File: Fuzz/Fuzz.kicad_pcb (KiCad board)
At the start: 2 copper layers, 13 parts, among them Q1 BC108, Q2 BC108, U3 TL071

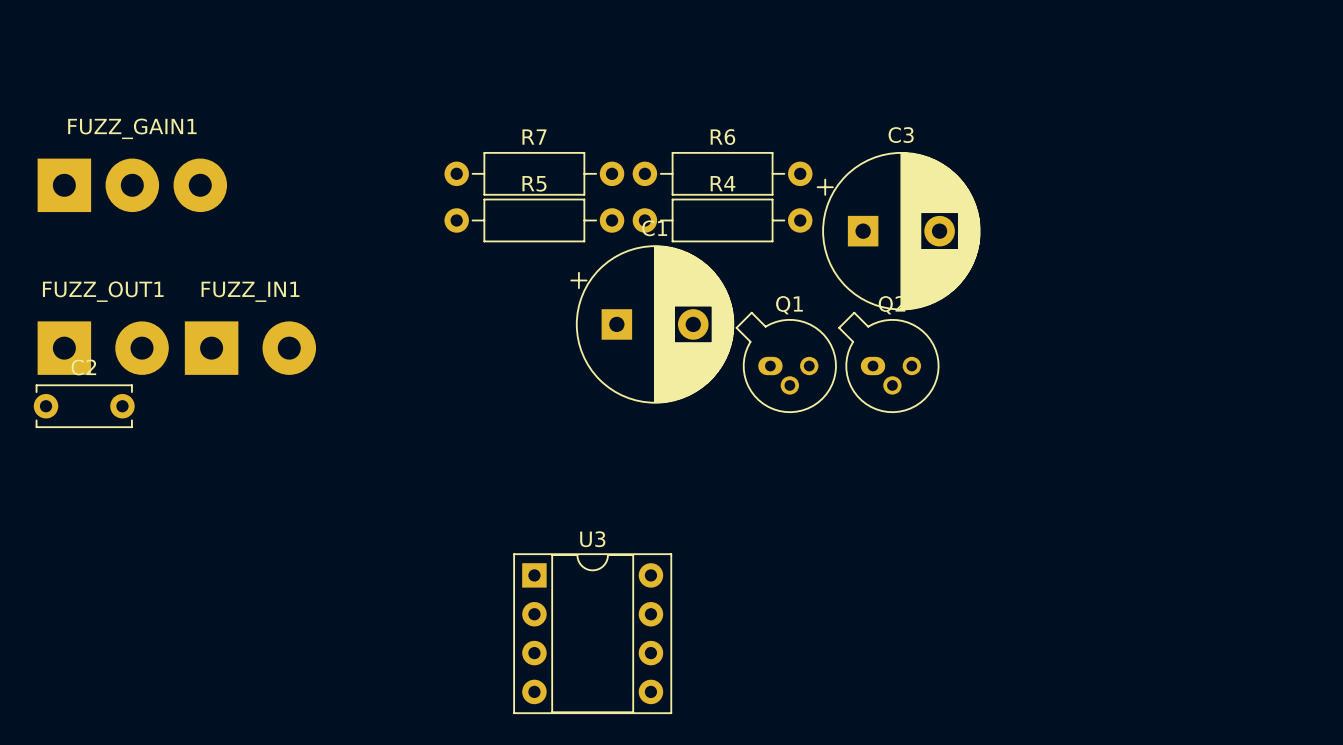
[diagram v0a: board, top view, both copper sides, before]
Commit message: Arrange pcb components
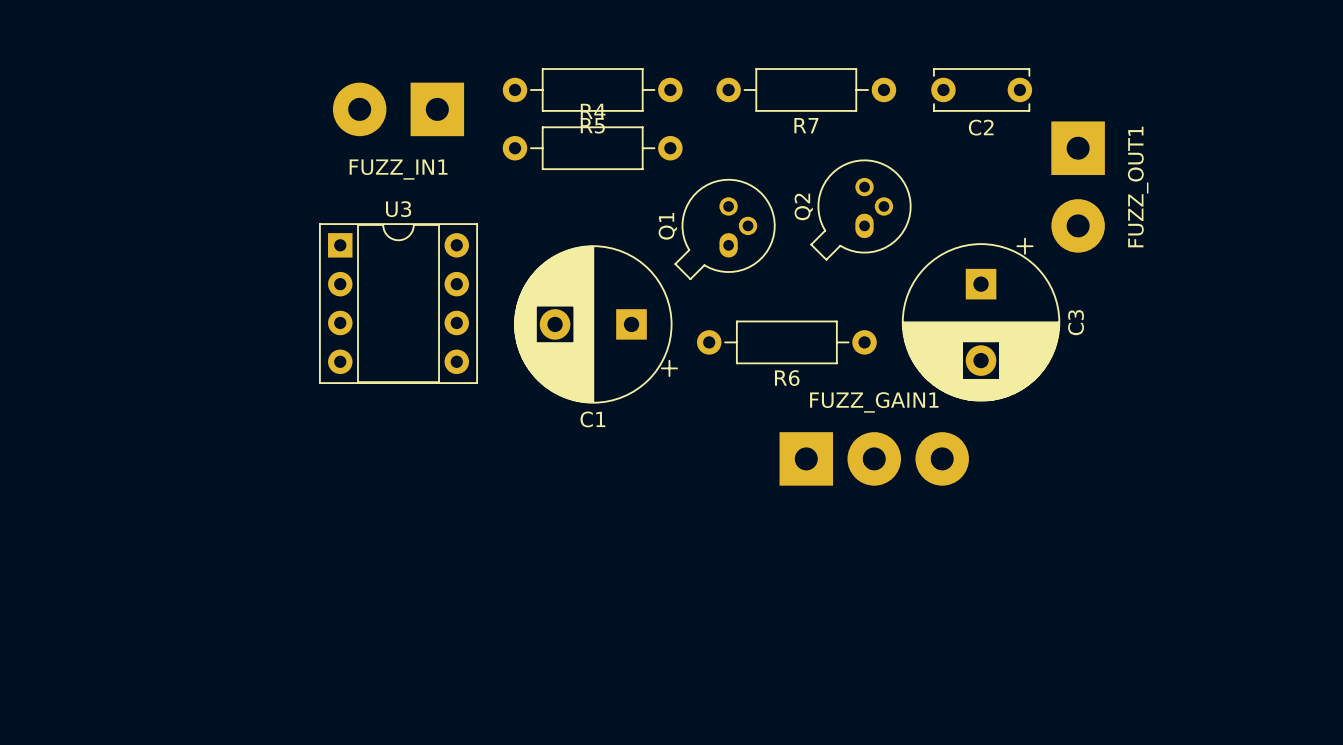
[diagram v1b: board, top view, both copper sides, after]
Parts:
- moved FUZZ_OUT1 67.6 mm to (69.8, 20.3), turned to 270 degrees
- moved C2 67.0 mm to (66.0, 16.5), turned to 180 degrees
- moved FUZZ_GAIN1 51.7 mm to (52.1, 40.6)
- moved R7 28.5 mm to (57.1, 16.5), turned to 180 degrees
- moved U3 25.0 mm to (21.6, 26.7)
- moved FUZZ_IN1 21.5 mm to (27.9, 17.8), turned to 180 degrees
- moved R6 18.1 mm to (55.9, 33.0), turned to 180 degrees
- moved R5 16.4 mm to (43.2, 16.5), turned to 180 degrees
- moved R4 9.72 mm to (33.0, 20.3)
- moved Q2 9.18 mm to (55.9, 25.4), turned to 90 degrees
- moved C3 8.45 mm to (63.5, 29.2), turned to 270 degrees
- moved Q1 8.35 mm to (47.0, 26.7), turned to 90 degrees
- moved C1 0.96 mm to (40.6, 31.8), turned to 180 degrees

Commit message: PCB tracks set
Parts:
- added J1: Conn_01x02_Male, Connector_Wire:SolderWirePad_1x02_P3.81mm_Drill1mm, F.Cu at (30.5, 19.1)
- moved FUZZ_IN1 11.4 mm to (17.8, 22.9), turned to 270 degrees
- moved FUZZ_OUT1 7.73 mm to (77.5, 21.6)
- moved R7 7.73 mm to (49.5, 17.8), turned to 0 degrees
- moved FUZZ_GAIN1 5.39 mm to (48.3, 44.5)
- moved C3 2.84 mm to (66.0, 30.5)
- moved Q2 2.84 mm to (58.4, 26.7)
- moved Q1 2.84 mm to (49.5, 27.9)
- moved R4 2.84 mm to (35.6, 21.6)
- moved R5 2.84 mm to (45.7, 17.8)
- moved U3 2.84 mm to (24.1, 27.9)
- moved R6 2.84 mm to (58.4, 34.3)
- moved C2 2.84 mm to (68.6, 17.8)
- moved C1 2.80 mm to (43.2, 33.0)
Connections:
- net +9V renamed Net-(J1-Pad1)
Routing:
- net GND: track 0.00 -> 101.9 mm
- net Net-(C2-Pad2): track 0.00 -> 27.8 mm
- net Net-(FUZZ_GAIN1-Pad1): track 0.00 -> 23.2 mm
- net Net-(J1-Pad1): track 0.00 -> 19.9 mm
- net Net-(C3-Pad1): track 0.00 -> 19.5 mm
- net Net-(Q1-Pad3): track 0.00 -> 15.5 mm
- net Net-(C1-Pad2): track 0.00 -> 15.1 mm
- net Net-(C1-Pad1): track 0.00 -> 14.3 mm
- net Net-(C2-Pad1): track 0.00 -> 11.6 mm
- net Net-(FUZZ_IN1-Pad2): track 0.00 -> 8.45 mm
- net Net-(Q2-Pad3): track 0.00 -> 6.88 mm
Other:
- board outline added: 72.4 x 38.1 mm

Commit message: Add PCB review components
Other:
- board text added: "Fuzz Effect"
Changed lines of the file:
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@@
   (general
     (thickness 1.6)
-    (drawings 4)
+    (drawings 5)
     (tracks 51)
     (zones 0)
@@
     (visible_elements FFFFFF7F)
     (pcbplotparams
-      (layerselection 0x010fc_ffffffff)
-      (usegerberextensions false)
+      (layerselection 0x010f0_ffffffff)
+      (usegerberextensions true)
       (usegerberattributes false)
       (usegerberadvancedattributes false)
@@
       (outputformat 1)
       (mirror false)
-      (drillshape 1)
+      (drillshape 0)
       (scaleselection 1)
-      (outputdirectory ""))
+      (outputdirectory "./"))
   )
   (net 0 "")
@@
     )
   )
+  (gr_text "Fuzz Effect" (at 21.59 46.99) (layer F.SilkS)
+    (effects (font (size 1.5 1.5) (thickness 0.3)))
+  )
   (gr_line (start 85.09 12.7) (end 12.7 12.7) (layer Edge.Cuts) (width 0.15))
   (gr_line (start 85.09 50.8) (end 85.09 12.7) (layer Edge.Cuts) (width 0.15))
@@
   (segment (start 58.42 24.13) (end 59.69 22.86) (width 0.25) (layer F.Cu) (net 8))
   (segment (start 59.69 22.86) (end 59.69 17.78) (width 0.25) (layer F.Cu) (net 8))
-  (segment (start 35.56 26.67) (end 35.56 21.59) (width 0.25) (layer F.Cu) (net 14))
-  (segment (start 31.75 30.48) (end 35.56 26.67) (width 0.25) (layer F.Cu) (net 14))
   (segment (start 48.26 42.44994) (end 50.06994 40.64) (width 0.25) (layer F.Cu) (net 9))
   (segment (start 48.26 44.45) (end 48.26 42.44994) (width 0.25) (layer F.Cu) (net 9))
@@
   (segment (start 22.86 33.02) (end 17.78 27.94) (width 0.25) (layer F.Cu) (net 12))
   (segment (start 24.13 33.02) (end 22.86 33.02) (width 0.25) (layer F.Cu) (net 12))
+  (segment (start 35.56 26.67) (end 35.56 21.59) (width 0.25) (layer F.Cu) (net 14))
+  (segment (start 31.75 30.48) (end 35.56 26.67) (width 0.25) (layer F.Cu) (net 14))
   (segment (start 34.29 19.05) (end 35.56 17.78) (width 0.25) (layer F.Cu) (net 14))
   (segment (start 30.48 19.05) (end 34.29 19.05) (width 0.25) (layer F.Cu) (net 14))
